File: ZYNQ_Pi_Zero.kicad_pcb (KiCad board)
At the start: 2 copper layers, 8 parts, among them Q501 2N7002, Q502 2N7002, Q503 2N7002, U301 W25Q256FVEI, U501 TPD4E05U06DQA, U502 TPD4E05U06DQA

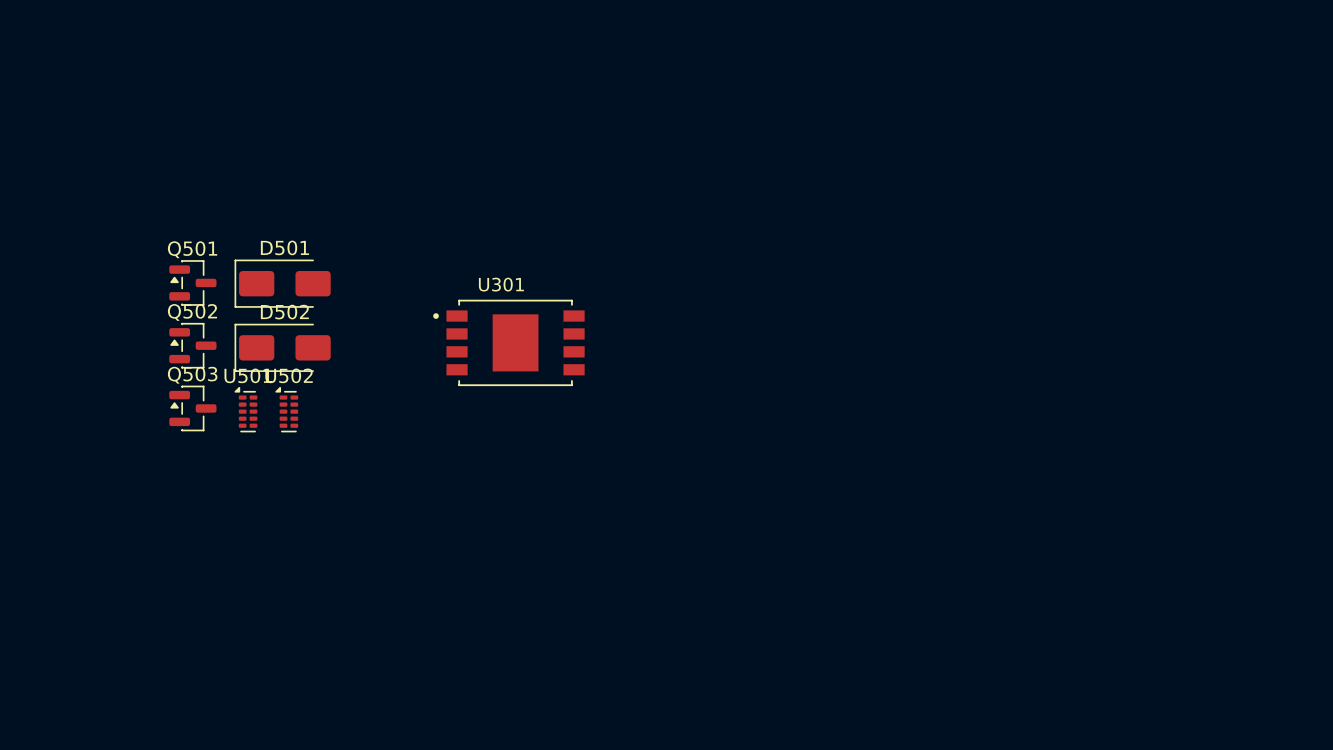
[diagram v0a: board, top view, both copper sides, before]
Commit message: feat: start to routing DDR3
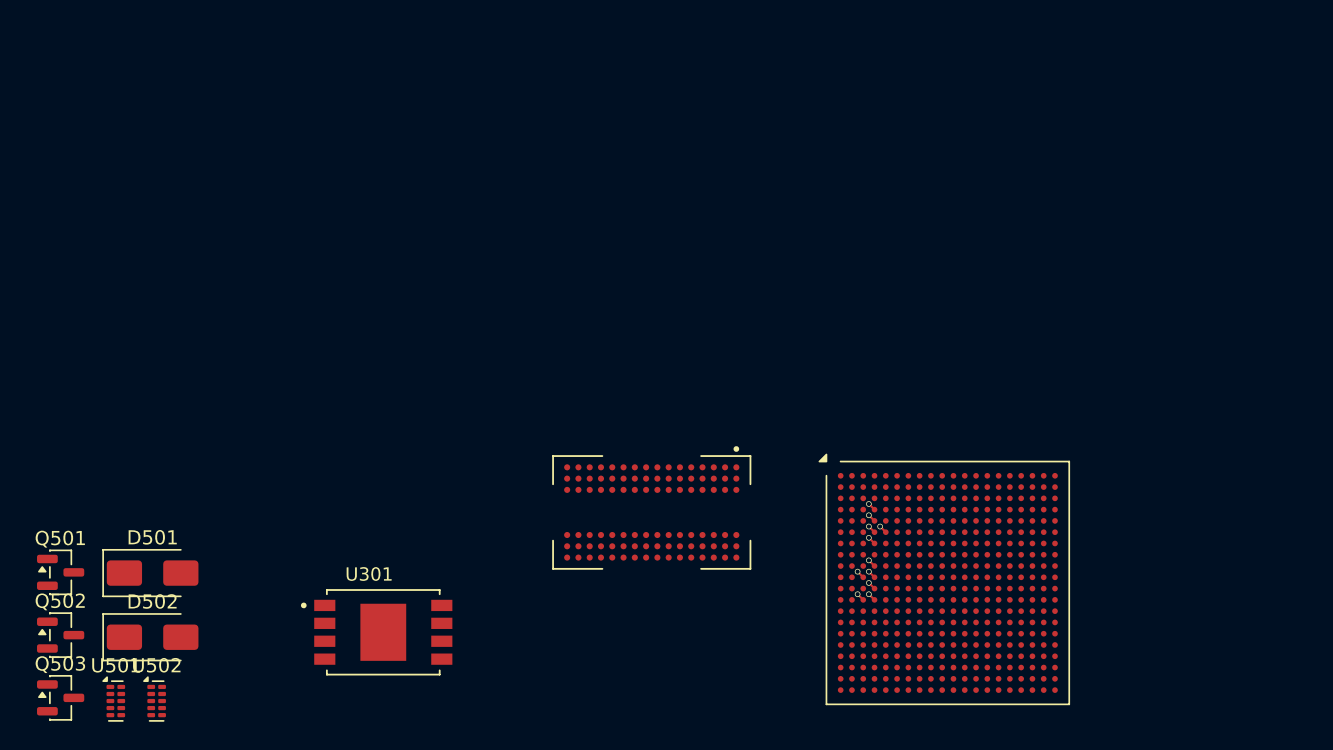
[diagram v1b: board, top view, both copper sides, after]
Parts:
- added U101: xc7z010clg400, Package_BGA:Xilinx_CLG400, F.Cu at (149.0, 100.0)
- added U201: MT41K256M16TW-107_P, Footprints:BGA96C80P9X16_1400X800X120, F.Cu at (128.0, 95.0)
- moved U301 22.6 mm to (109.0, 103.5)
- moved U501 22.6 mm to (90.0, 108.4)
- moved Q501 22.6 mm to (86.1, 99.2)
- moved Q502 22.6 mm to (86.1, 103.7)
- moved Q503 22.6 mm to (86.1, 108.2)
- moved U502 22.6 mm to (92.9, 108.4)
- moved D501 22.6 mm to (92.6, 99.3)
- moved D502 22.6 mm to (92.6, 103.8)
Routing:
- net /DDR3/DDR_A6: track 0.00 -> 0.57 mm, vias 0 -> 1
- net /DDR3/DDR_A4: track 0.00 -> 0.57 mm, vias 0 -> 1
- net /DDR3/DDR_A2: track 0.00 -> 0.57 mm, vias 0 -> 1
- net /DDR3/DDR_A14: track 0.00 -> 0.57 mm, vias 0 -> 1
- net /DDR3/DDR_A11: track 0.00 -> 0.57 mm, vias 0 -> 1
- net /DDR3/DDR_A10: track 0.00 -> 0.57 mm, vias 0 -> 1
- net /DDR3/DDR_A9: track 0.00 -> 0.57 mm, vias 0 -> 1
- net /DDR3/DDR_A7: track 0.00 -> 0.57 mm, vias 0 -> 1
- net /DDR3/DDR_A3: track 0.00 -> 0.57 mm, vias 0 -> 1
- net /DDR3/DDR_A13: track 0.00 -> 0.57 mm, vias 0 -> 1
- net /DDR3/DDR_A12: track 0.00 -> 0.57 mm, vias 0 -> 1
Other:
- copper layers 2 -> 4

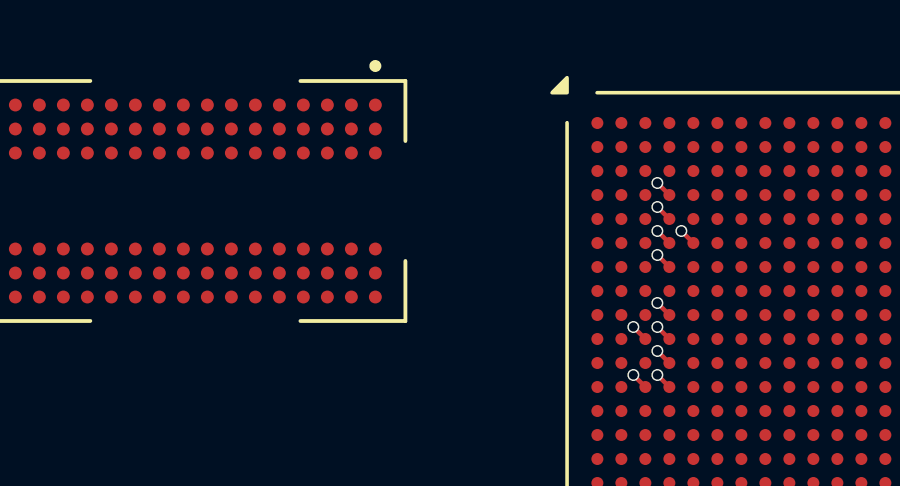
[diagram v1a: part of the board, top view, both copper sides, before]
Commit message: feat: continue to routing DDR3
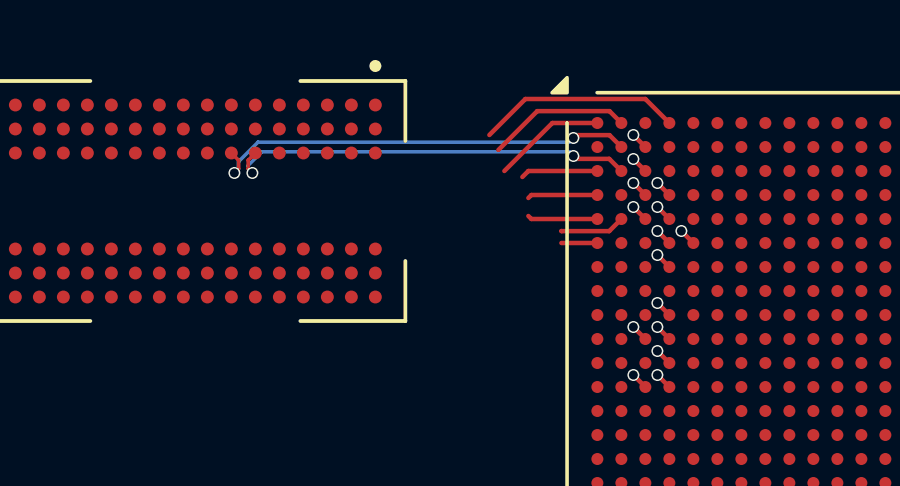
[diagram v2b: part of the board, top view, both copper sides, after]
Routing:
- net /DDR3/DDR_DQS0_N: track 0.00 -> 14.6 mm, vias 0 -> 2
- net /DDR3/DDR_DQS0_P: track 0.00 -> 14.0 mm, vias 0 -> 2
- net /DDR3/DDR_D3: track 0.00 -> 6.83 mm
- net /DDR3/DDR_D2: track 0.00 -> 4.80 mm
- net /DDR3/DDR_DM0: track 0.00 -> 3.76 mm
- net /DDR3/DDR_D6: track 0.00 -> 2.58 mm
- net /DDR3/DDR_D5: track 0.00 -> 2.34 mm
- net /DDR3/DDR_D7: track 0.00 -> 2.34 mm
- net /DDR3/DDR_D8: track 0.00 -> 2.17 mm
- net /DDR3/DDR_DM1: track 0.00 -> 1.20 mm
- net /DDR3/DDR_D1: track 0.00 -> 0.57 mm, vias 0 -> 1
- net /DDR3/DDR_D0: track 0.00 -> 0.57 mm, vias 0 -> 1
- net /DDR3/DDR_D9: track 0.00 -> 0.57 mm, vias 0 -> 1
- net /DDR3/DDR_D4: track 0.00 -> 0.57 mm, vias 0 -> 1

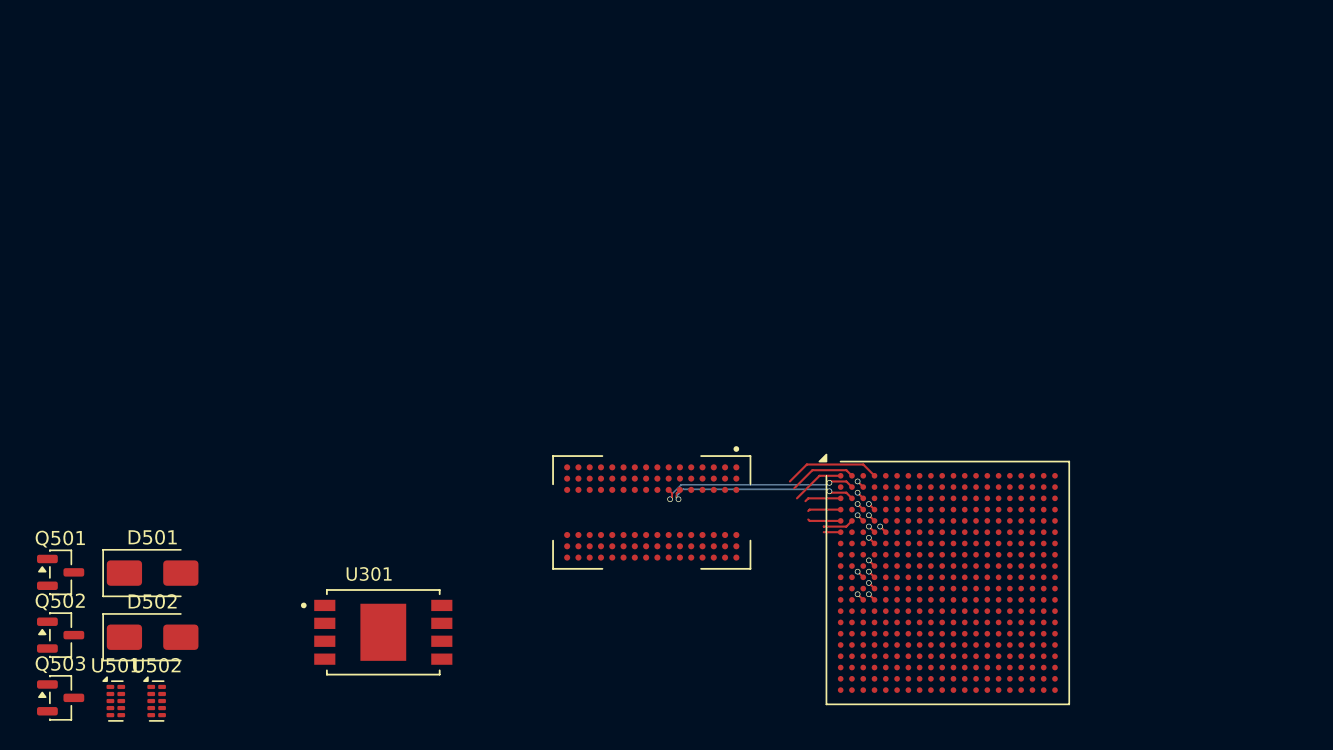
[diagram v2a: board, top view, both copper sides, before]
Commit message: feat: restart routing ddr
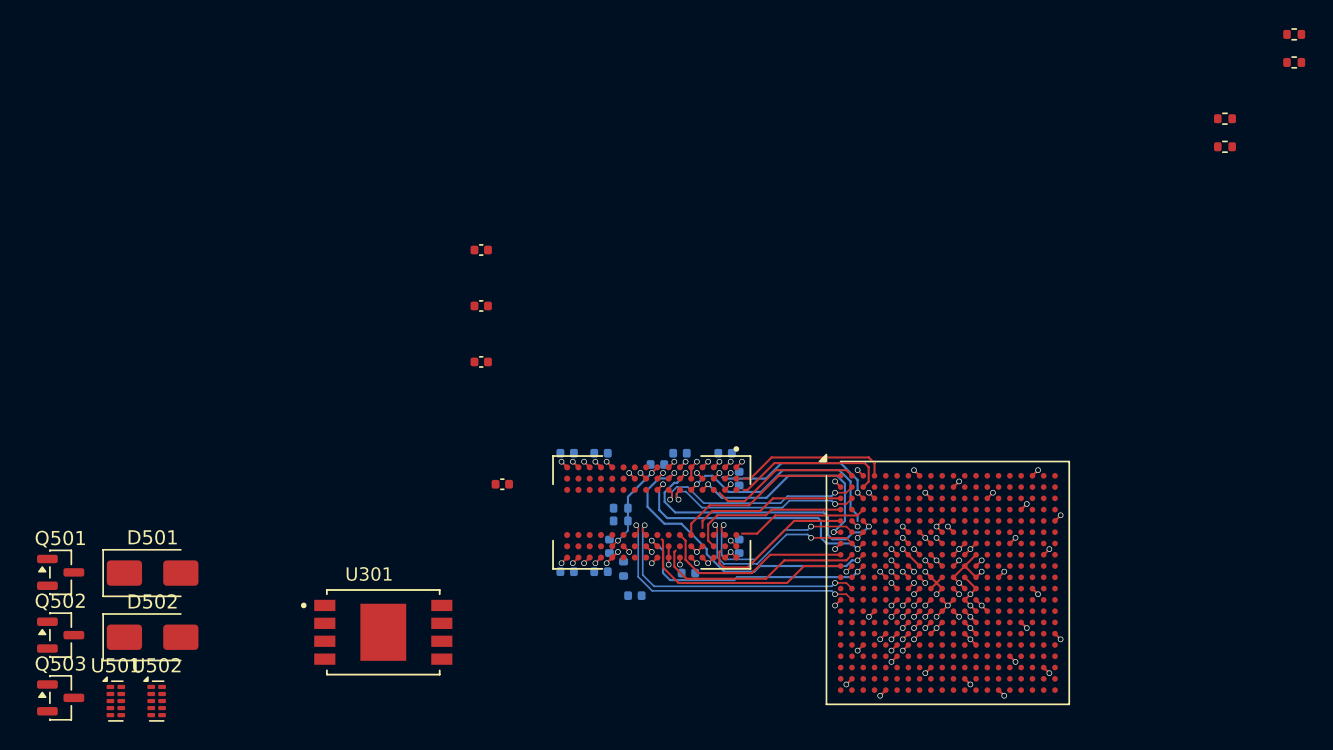
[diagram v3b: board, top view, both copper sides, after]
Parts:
- added C201: 100n, Capacitor_SMD:C_0402_1005Metric, B.Cu at (133.2, 90.8)
- added C202: 100n, Capacitor_SMD:C_0402_1005Metric, B.Cu at (130.0, 90.8)
- added C203: 100n, Capacitor_SMD:C_0402_1005Metric, B.Cu at (124.4, 90.8)
- added C204: 100n, Capacitor_SMD:C_0402_1005Metric, B.Cu at (130.6, 99.3)
- added C205: 100n, Capacitor_SMD:C_0402_1005Metric, B.Cu at (128.4, 91.6)
- added C206: 100n, Capacitor_SMD:C_0402_1005Metric, F.Cu at (117.4, 93.0)
- added C208: 100n, Capacitor_SMD:C_0402_1005Metric, B.Cu at (125.0, 97.4)
- added C209: 100n, Capacitor_SMD:C_0402_1005Metric, B.Cu at (124.4, 99.2)
- added C210: 100n, Capacitor_SMD:C_0402_1005Metric, B.Cu at (126.8, 100.9)
- added C211: 100n, Capacitor_SMD:C_0402_1005Metric, B.Cu at (134.2, 97.4)
- added C212: 100n, Capacitor_SMD:C_0402_1005Metric, B.Cu at (134.2, 92.6)
- added C213: 100n, Capacitor_SMD:C_0402_1005Metric, B.Cu at (122.0, 90.8)
- added C214: 100n, Capacitor_SMD:C_0402_1005Metric, B.Cu at (122.0, 99.2)
- added C303: 100n, Capacitor_SMD:C_0402_1005Metric, F.Cu at (115.9, 80.4)
- added C413: 100n, Capacitor_SMD:C_0402_1005Metric, F.Cu at (115.9, 84.3)
- added C602: 100n, Capacitor_SMD:C_0402_1005Metric, F.Cu at (115.9, 76.4)
- added R201: 240R, Resistor_SMD:R_0402_1005Metric, B.Cu at (126.0, 99.0)
- added R202: 10k, Resistor_SMD:R_0402_1005Metric, B.Cu at (125.8, 95.6)
- added R203: 10k, Resistor_SMD:R_0402_1005Metric, B.Cu at (125.8, 94.7)
- added R402: 10k, Resistor_SMD:R_0402_1005Metric, F.Cu at (173.6, 61.1)
- added R407: 10k, Resistor_SMD:R_0402_1005Metric, F.Cu at (173.6, 63.1)
- added R516: 10k, Resistor_SMD:R_0402_1005Metric, F.Cu at (168.7, 67.1)
- added R517: 10k, Resistor_SMD:R_0402_1005Metric, F.Cu at (168.7, 69.1)
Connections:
- U101 pad B4: /DDR3/DDR_RESET -> /DDR3/DDR_~{RESET}
- U101 pad M5: /DDR3/DDR_WE -> /DDR3/DDR_~{WE}
- U101 pad N1: /DDR3/DDR_S0 -> /DDR3/DDR_~{CS}
- U101 pad P4: /DDR3/DDR_RAS -> /DDR3/DDR_~{RAS}
- U101 pad P5: /DDR3/DDR_CAS -> /DDR3/DDR_~{CAS}
- U201 pad A9: VSS -> GND
- U201 pad B1: VSSQ -> GND
- U201 pad B3: VSS -> GND
- U201 pad B9: VSSQ -> GND
- U201 pad D1: VSSQ -> GND
- U201 pad D8: VSSQ -> GND
- U201 pad E1: VSS -> GND
- U201 pad E2: VSSQ -> GND
- U201 pad E8: VSSQ -> GND
- U201 pad F9: VSSQ -> GND
- U201 pad G1: VSSQ -> GND
- U201 pad G8: VSS -> GND
- U201 pad G9: VSSQ -> GND
- U201 pad J2: VSS -> GND
- U201 pad J8: VSS -> GND
- U201 pad M1: VSS -> GND
- U201 pad M9: VSS -> GND
- U201 pad P1: VSS -> GND
- U201 pad P9: VSS -> GND
- U201 pad T1: VSS -> GND
- U201 pad T9: VSS -> GND
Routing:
- net GND: track 0.00 -> 55.2 mm, vias 0 -> 71
- net /DDR3/DDR_D15: track 0.00 -> 31.8 mm, vias 0 -> 1
- net /DDR3/DDR_D11: track 0.00 -> 21.7 mm, vias 0 -> 2
- net /DDR3/DDR_CLK_N: track 0.00 -> 20.4 mm, vias 0 -> 2
- net /DDR3/DDR_CLK_P: track 0.00 -> 19.9 mm, vias 0 -> 2
- net /DDR3/DDR_D9: track 0.57 -> 20.2 mm, vias 1 -> 2
- net /DDR3/DDR_D10: track 0.00 -> 18.6 mm, vias 0 -> 2
- net /DDR3/DDR_D12: track 0.00 -> 17.0 mm, vias 0 -> 1
- net /DDR3/DDR_D13: track 0.00 -> 15.4 mm, vias 0 -> 1
- net /DDR3/DDR_DM1: track 1.20 -> 15.8 mm, vias 0 -> 2
- net /DDR3/DDR_DQS1_P: track 0.00 -> 14.1 mm, vias 0 -> 2
- net /DDR3/DDR_D14: track 0.00 -> 13.9 mm
- net /DDR3/DDR_DQS1_N: track 0.00 -> 13.6 mm, vias 0 -> 2
- net /DDR3/DDR_D0: track 0.57 -> 12.1 mm
- net /DDR3/DDR_D1: track 0.57 -> 11.4 mm, vias 1 -> 0
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
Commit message: feat: continue routing dd3
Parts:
- moved C210 0.71 mm to (126.1, 100.8)
- moved R202 0.70 mm to (125.1, 95.6)
- moved R203 0.70 mm to (125.1, 94.7)
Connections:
- U201 pad A2: /DDR3/DDR_D2 -> /DDR3/DDR_D3
- U201 pad A3: /DDR3/DDR_D0 -> /DDR3/DDR_D1
- U201 pad A7: /DDR3/DDR_D3 -> /DDR3/DDR_D4
- U201 pad B8: /DDR3/DDR_D1 -> /DDR3/DDR_D7
- U201 pad C2: /DDR3/DDR_D4 -> /DDR3/DDR_D0
- U201 pad C3: /DDR3/DDR_D6 -> /DDR3/DDR_D2
- U201 pad D7: /DDR3/DDR_D7 -> /DDR3/DDR_D6
- U201 pad E3: /DDR3/DDR_D15 -> /DDR3/DDR_D8
- U201 pad F2: /DDR3/DDR_D13 -> /DDR3/DDR_D9
- U201 pad F8: /DDR3/DDR_D12 -> /DDR3/DDR_D13
- U201 pad G2: /DDR3/DDR_D9 -> /DDR3/DDR_D11
- U201 pad H3: /DDR3/DDR_D11 -> /DDR3/DDR_D10
- U201 pad H7: /DDR3/DDR_D8 -> /DDR3/DDR_D15
- U201 pad H8: /DDR3/DDR_D10 -> /DDR3/DDR_D12
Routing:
- net /DDR3/DDR_A11: track 0.00 -> 40.6 mm, vias 0 -> 2
- net /DDR3/DDR_~{CAS}: track 0.00 -> 40.4 mm, vias 0 -> 1
- net /DDR3/DDR_A7: track 0.00 -> 38.6 mm, vias 0 -> 2
- net /DDR3/DDR_A14: track 0.00 -> 37.8 mm, vias 0 -> 4
- net /DDR3/DDR_~{RAS}: track 0.00 -> 37.4 mm, vias 0 -> 1
- net /DDR3/DDR_A9: track 0.00 -> 35.7 mm, vias 0 -> 2
- net /DDR3/DDR_~{WE}: track 0.00 -> 35.6 mm, vias 0 -> 1
- net /DDR3/DDR_A0: track 0.00 -> 35.3 mm
- net /DDR3/DDR_~{CS}: track 0.00 -> 34.5 mm
- net /DDR3/DDR_ODT: track 0.00 -> 31.7 mm, vias 0 -> 1
- net /DDR3/DDR_A5: track 0.00 -> 30.9 mm, vias 0 -> 2
- net /DDR3/DDR_A13: track 0.00 -> 29.7 mm, vias 0 -> 2
- net /DDR3/DDR_A12: track 0.00 -> 28.8 mm, vias 0 -> 2
- net /DDR3/DDR_~{RESET}: track 0.00 -> 27.9 mm
- net /DDR3/DDR_A10: track 0.00 -> 27.9 mm, vias 0 -> 2
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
